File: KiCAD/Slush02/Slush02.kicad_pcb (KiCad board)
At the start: 2 copper layers, 32 x 62 mm, 72 parts, among them IC1 ADR440ARMZ, IC10 AD8237ARMZ, IC11 AD8276ARMZ, IC12 AD8603AUJZ-R2, IC13 AD8237ARMZ, IC14 LM78L05, IC15 ADS1115, IC2 AD8276ARMZ, IC3 AD8603AUJZ-R2, IC4 AD8237ARMZ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

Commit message: more routing work on Slush02
moved ground plane to bottom layer
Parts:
- moved R14 7.93 mm to (56.8, 81.0)
- moved R10 7.84 mm to (55.5, 81.0)
- moved J2 7.00 mm to (70.0, 75.9)
- moved R18 7.00 mm to (83.4, 80.1)
- moved R22 7.00 mm to (81.4, 80.1)
- moved C10 2.00 mm to (60.5, 100.9)
- moved C11 2.00 mm to (60.9, 99.4)
- moved C12 2.00 mm to (60.5, 92.9)
- moved C13 2.00 mm to (60.5, 97.9)
- moved C14 2.00 mm to (65.2, 91.4)
- moved C15 2.00 mm to (66.3, 90.4)
- moved C16 2.00 mm to (65.2, 89.4)
- moved C17 2.00 mm to (60.5, 87.9)
- moved C18 2.00 mm to (60.9, 86.4)
- moved C19 2.00 mm to (79.5, 104.2)
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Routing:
- net /Power: track 26.0 -> 72.5 mm
- net /Channel0/out: track 0.65 -> 38.9 mm, vias 0 -> 1
- net GNDA: track 0.00 -> 36.8 mm, vias 0 -> 16
- net /Channel3/out: track 0.65 -> 32.9 mm, vias 0 -> 2
- net /Channel1/out: track 0.65 -> 25.3 mm, vias 0 -> 2
- net /1V: track 0.00 -> 24.5 mm, vias 0 -> 3
- net /Channel1/Vpower: track 11.5 -> 30.0 mm
- net /Channel3/Vpower: track 11.5 -> 30.0 mm
- net /Channel2/out: track 0.65 -> 19.0 mm, vias 0 -> 2
- net /Channel2/Vpower: track 11.5 -> 29.4 mm
- net /Channel0/Vpower: track 11.5 -> 29.3 mm
- net /Channel2/I-: track 0.00 -> 17.5 mm
- net /Channel1/V-: track 18.4 -> 31.4 mm
- net /Channel2/V+: track 15.6 -> 28.2 mm
- net /Channel2/I+: track 3.56 -> 15.3 mm, vias 0 -> 1
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- added copper zone on F.Cu, net GND
- added copper zone on B.Cu, net GNDA
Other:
- board size 32 x 62 mm -> 32 x 55 mm
- rule via_min_size: 0.4 -> 0.3
- board text added: "Dylan Oh"
- board text added: "Sep 2019"
- board text added: "Slush02"

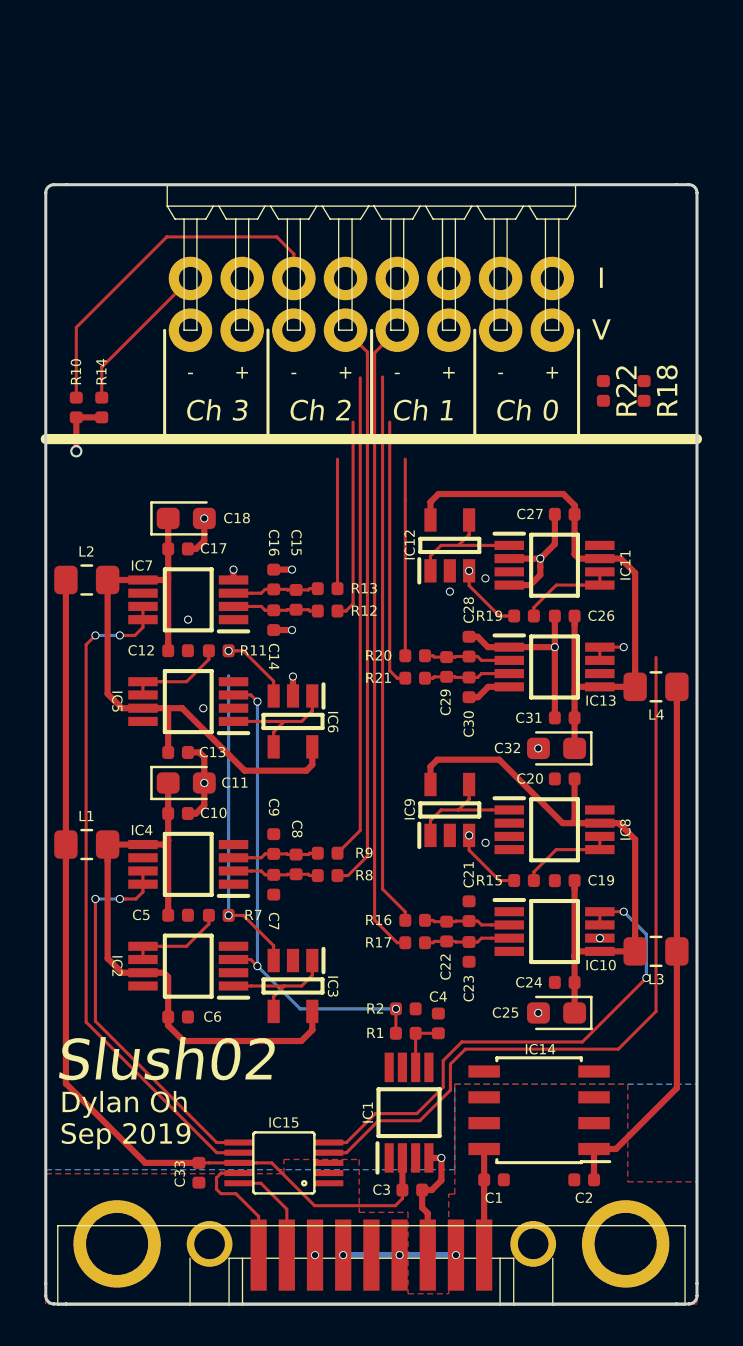
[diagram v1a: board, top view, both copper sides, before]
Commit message: fixed ground connectivity on Slush02
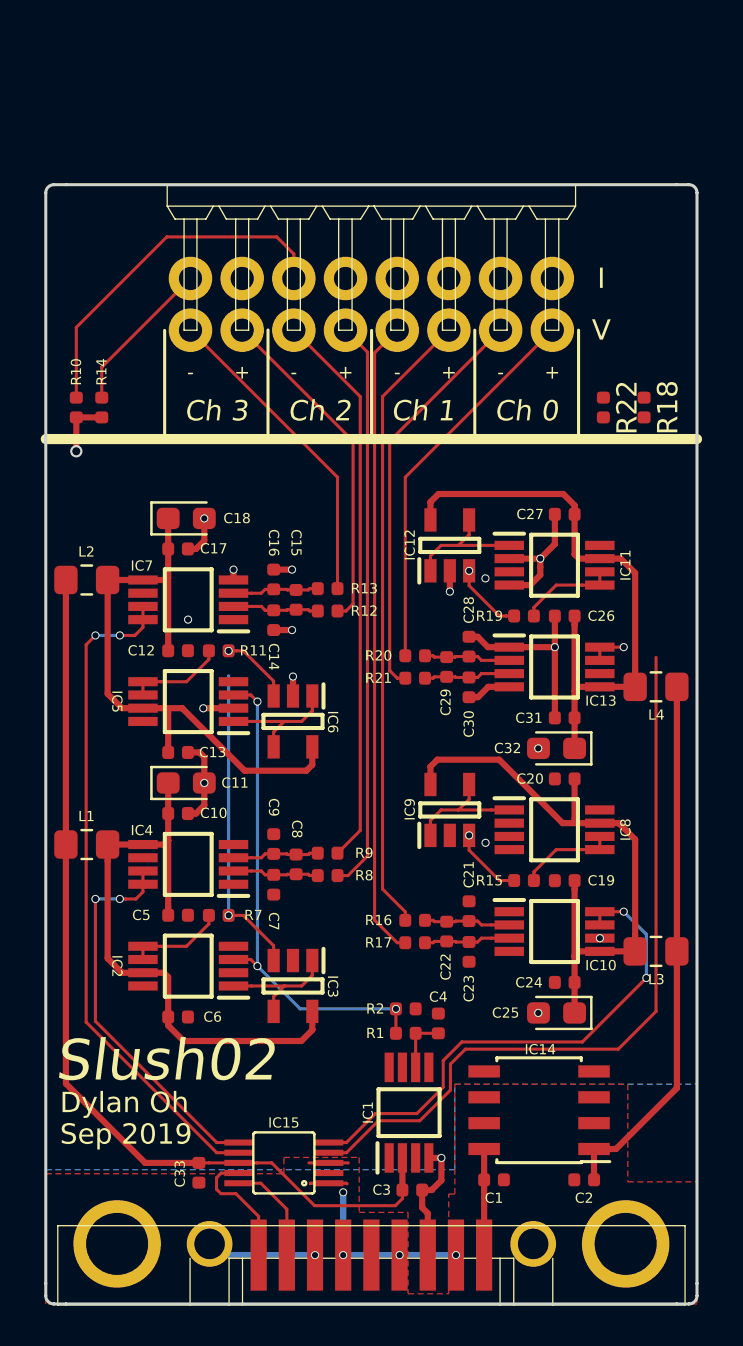
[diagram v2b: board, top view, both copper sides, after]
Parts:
- moved R18 0.81 mm to (83.4, 81.0)
- moved R22 0.81 mm to (81.4, 81.0)
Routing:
- net GND: track 5.54 -> 17.8 mm, vias 4 -> 5
- net /Channel0/V+: track 9.66 -> 19.0 mm
- net /Channel3/V-: track 6.36 -> 15.7 mm
- net /Channel3/V+: track 9.84 -> 16.6 mm
- net /Channel0/V-: track 13.1 -> 19.9 mm
- net /Channel2/V-: track 23.8 -> 27.5 mm
- net /Channel1/V+: track 27.2 -> 30.8 mm
- net GNDA: track 36.8 -> 39.3 mm
